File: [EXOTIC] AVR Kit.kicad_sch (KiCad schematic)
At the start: 20 parts, among them J2 AVR-ISP-10, J3 USB_B, J4 Conn_01x08_Socket, J5 Conn_01x08_Socket, J6 Conn_01x09_Socket, J7 Conn_01x07_Socket, SW1 SW_Push, U1 ATmega32A-P, U6 CH340C, Y1 16 MHz

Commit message: Update [EXOTIC] AVR Kit.kicad_sch
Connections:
- net PC0: now also J6.2 (Pin_2); no longer J6.8 (Pin_8)
- net PC1: now also J6.3 (Pin_3); no longer J6.7 (Pin_7)
- net PC6: now also J6.8 (Pin_8); no longer J6.2 (Pin_2)
- net PC7: now also J6.9 (Pin_9); no longer J6.1 (Pin_1)
- net PD7: now also J6.1 (Pin_1); no longer J6.9 (Pin_9)
- net TCK: now also J6.4 (Pin_4); no longer J6.6 (Pin_6)
- net TDI: now also J6.7 (Pin_7); no longer J6.3 (Pin_3)
- net TDO: now also J6.6 (Pin_6); no longer J6.4 (Pin_4)
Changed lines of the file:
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@@
     )
   )
-  (symbol (lib_id "Connector:Conn_01x09_Socket") (at 110.49 106.68 0) (mirror x) (unit 1)
-    (in_bom yes) (on_board yes) (dnp no) (fields_autoplaced)
-    (property "Reference" "J6" (at 111.76 105.41 0)
+  (symbol (lib_id "Connector:Conn_01x09_Socket") (at 110.49 106.68 0) (unit 1)
+    (in_bom yes) (on_board yes) (dnp no)
+    (property "Reference" "J6" (at 111.76 107.95 0)
       (effects (font (size 1.27 1.27)) (justify left))
     )
-    (property "Value" "Conn_01x09_Socket" (at 111.76 107.95 0)
+    (property "Value" "Conn_01x09_Socket" (at 111.76 105.41 0)
       (effects (font (size 1.27 1.27)) (justify left))
     )

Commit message: WIP
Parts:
- added J8: ICSP_Connector, Connector_PinHeader_2.54mm:PinHeader_2x03_P2.54mm_Vertical, symbol PCM_SL_Connectors:ICSP_Connector
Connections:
- net +5V: now also J8.2 (VCC)
- net GND: now also J8.6 (GND)
- net MISO: now also J8.1 (MISO)
- net MOSI: now also J8.4 (MOSI)
- net SCK: now also J8.3 (SCK)
- net ~{RESET}: now also J8.5 (~{RST})
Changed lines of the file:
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@@
+    (stroke (width 0) (type default))
+  )
+  (wire (pts (xy 189.23 52.07) (xy 191.77 52.07))
     (stroke (width 0) (type default))
   )
@@
     (stroke (width 0) (type default))
   )
+  (wire (pts (xy 210.82 46.99) (xy 208.28 46.99))
+    (stroke (width 0) (type default))
+  )
   (wire (pts (xy 91.44 111.76) (xy 105.41 111.76))
     (stroke (width 0) (type default))
@@
     (stroke (width 0) (type default))
   )
+  (wire (pts (xy 210.82 52.07) (xy 208.28 52.07))
+    (stroke (width 0) (type default))
+  )
   (wire (pts (xy 76.2 147.32) (xy 76.2 148.59))
     (stroke (width 0) (type default))
@@
     (stroke (width 0) (type default))
   )
+  (wire (pts (xy 189.23 46.99) (xy 191.77 46.99))
+    (stroke (width 0) (type default))
+  )
   (wire (pts (xy 58.42 44.45) (xy 60.96 44.45))
     (stroke (width 0) (type default))
@@
     (stroke (width 0) (type default))
   )
+  (wire (pts (xy 189.23 49.53) (xy 191.77 49.53))
+    (stroke (width 0) (type default))
+  )
   (wire (pts (xy 154.94 115.57) (xy 157.48 115.57))
     (stroke (width 0) (type default))
@@
   )
   (wire (pts (xy 91.44 101.6) (xy 105.41 101.6))
+    (stroke (width 0) (type default))
+  )
+  (wire (pts (xy 210.82 49.53) (xy 208.28 49.53))
     (stroke (width 0) (type default))
   )
@@
     (effects (font (size 1.27 1.27)) (justify left bottom))
   )
+  (label "MOSI" (at 210.82 49.53 0) (fields_autoplaced)
+    (effects (font (size 1.27 1.27)) (justify left bottom))
+  )
   (label "PD7" (at 101.6 96.52 0) (fields_autoplaced)
     (effects (font (size 1.27 1.27)) (justify left bottom))
@@
     (effects (font (size 1.27 1.27)) (justify left bottom))
   )
+  (label "SCK" (at 189.23 49.53 180) (fields_autoplaced)
+    (effects (font (size 1.27 1.27)) (justify right bottom))
+  )
   (label "PA3" (at 93.98 60.96 0) (fields_autoplaced)
     (effects (font (size 1.27 1.27)) (justify left bottom))
@@
   (label "PA4" (at 93.98 63.5 0) (fields_autoplaced)
     (effects (font (size 1.27 1.27)) (justify left bottom))
+  )
+  (label "MISO" (at 189.23 46.99 180) (fields_autoplaced)
+    (effects (font (size 1.27 1.27)) (justify right bottom))
   )
   (label "TDO" (at 93.98 109.22 0) (fields_autoplaced)
@@
   (label "PB1" (at 93.98 78.74 0) (fields_autoplaced)
     (effects (font (size 1.27 1.27)) (justify left bottom))
+  )
+  (label "~{RESET}" (at 189.23 52.07 180) (fields_autoplaced)
+    (effects (font (size 1.27 1.27)) (justify right bottom))
   )
   (label "~{RESET}" (at 55.88 53.34 180) (fields_autoplaced)
@@
     )
   )
+  (symbol (lib_id "PCM_SL_Connectors:ICSP_Connector") (at 199.39 49.53 0) (unit 1)
+    (in_bom yes) (on_board yes) (dnp no) (fields_autoplaced)
+    (property "Reference" "J8" (at 201.93 39.37 0)
+      (effects (font (size 1.27 1.27)))
+    )
+    (property "Value" "ICSP_Connector" (at 201.93 41.91 0)
+      (effects (font (size 1.27 1.27)))
+    )
+    (property "Footprint" "Connector_PinHeader_2.54mm:PinHeader_2x03_P2.54mm_Vertical" (at 195.58 46.99 0)
+      (effects (font (size 1.27 1.27)) hide)
+    )
+    (property "Datasheet" "" (at 195.58 46.99 0)
+      (effects (font (size 1.27 1.27)) hide)
+    )
+    (pin "3")
+    (pin "6")
+    (pin "5")
+    (pin "1")
+    (pin "4")
+    (pin "2")
+    (instances
+      (project "[EXOTIC] AVR Kit"
+        (path "/bd689b4b-40d7-46ba-91b6-965ce30f8212"
+          (reference "J8") (unit 1)
+        )
+      )
+    )
+  )
   (symbol (lib_id "Device:R") (at 60.96 35.56 0) (unit 1)
     (in_bom yes) (on_board yes) (dnp no) (fields_autoplaced)
@@
     )
   )
+  (symbol (lib_id "power:GND") (at 210.82 52.07 0) (unit 1)
+    (in_bom yes) (on_board yes) (dnp no) (fields_autoplaced)
+    (property "Reference" "#PWR033" (at 210.82 58.42 0)
+      (effects (font (size 1.27 1.27)) hide)
+    )
+    (property "Value" "GND" (at 210.82 57.15 0)
+      (effects (font (size 1.27 1.27)))
+    )
+    (property "Footprint" "" (at 210.82 52.07 0)
+      (effects (font (size 1.27 1.27)) hide)
+    )
+    (property "Datasheet" "" (at 210.82 52.07 0)
+      (effects (font (size 1.27 1.27)) hide)
+    )
+    (pin "1")
+    (instances
+      (project "[EXOTIC] AVR Kit"
+        (path "/bd689b4b-40d7-46ba-91b6-965ce30f8212"
+          (reference "#PWR033") (unit 1)
+        )
+      )
+      (project "ATMEGA32A Development Board"
+        (path "/e232854a-3fe0-4443-9abe-081b69d86c79"
+          (reference "#PWR018") (unit 1)
+        )
+      )
+    )
+  )
   (symbol (lib_id "Connector:USB_B") (at 199.39 102.87 0) (mirror y) (unit 1)
     (in_bom yes) (on_board yes) (dnp no)
@@
         )
       )
+    )
+  )
+  (symbol (lib_id "power:+5V") (at 210.82 46.99 0) (unit 1)
+    (in_bom yes) (on_board yes) (dnp no) (fields_autoplaced)
+    (property "Reference" "#PWR032" (at 210.82 50.8 0)
+      (effects (font (size 1.27 1.27)) hide)
+    )
+    (property "Value" "+5V" (at 210.82 43.18 0)
+      (effects (font (size 1.27 1.27)))
+    )
+    (property "Footprint" "" (at 210.82 46.99 0)
+      (effects (font (size 1.27 1.27)) hide)
+    )
+    (property "Datasheet" "" (at 210.82 46.99 0)
+      (effects (font (size 1.27 1.27)) hide)
+    )
+    (pin "1")
+    (instances
+      (project "[EXOTIC] AVR Kit"
+        (path "/bd689b4b-40d7-46ba-91b6-965ce30f8212"
+          (reference "#PWR032") (unit 1)
+        )
+      )
+      (project "ATMEGA32A Development Board"
+        (path "/e232854a-3fe0-4443-9abe-081b69d86c79"
+          (reference "#PWR012") (unit 1)
+        )
+      )

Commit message: Rev. 3
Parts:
- removed J8: ICSP_Connector, Connector_PinHeader_2.54mm:PinHeader_2x03_P2.54mm_Vertical, symbol PCM_SL_Connectors:ICSP_Connector
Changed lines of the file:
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@@
-    (stroke (width 0) (type default))
-  )
-  (wire (pts (xy 189.23 52.07) (xy 191.77 52.07))
     (stroke (width 0) (type default))
   )
@@
     (stroke (width 0) (type default))
   )
-  (wire (pts (xy 210.82 46.99) (xy 208.28 46.99))
-    (stroke (width 0) (type default))
-  )
   (wire (pts (xy 91.44 111.76) (xy 105.41 111.76))
     (stroke (width 0) (type default))
@@
     (stroke (width 0) (type default))
   )
-  (wire (pts (xy 210.82 52.07) (xy 208.28 52.07))
-    (stroke (width 0) (type default))
-  )
   (wire (pts (xy 76.2 147.32) (xy 76.2 148.59))
     (stroke (width 0) (type default))
@@
     (stroke (width 0) (type default))
   )
-  (wire (pts (xy 189.23 46.99) (xy 191.77 46.99))
-    (stroke (width 0) (type default))
-  )
   (wire (pts (xy 58.42 44.45) (xy 60.96 44.45))
     (stroke (width 0) (type default))
@@
     (stroke (width 0) (type default))
   )
-  (wire (pts (xy 189.23 49.53) (xy 191.77 49.53))
-    (stroke (width 0) (type default))
-  )
   (wire (pts (xy 154.94 115.57) (xy 157.48 115.57))
     (stroke (width 0) (type default))
@@
   )
   (wire (pts (xy 91.44 101.6) (xy 105.41 101.6))
-    (stroke (width 0) (type default))
-  )
-  (wire (pts (xy 210.82 49.53) (xy 208.28 49.53))
     (stroke (width 0) (type default))
   )
@@
     (effects (font (size 1.27 1.27)) (justify left bottom))
   )
-  (label "MOSI" (at 210.82 49.53 0) (fields_autoplaced)
-    (effects (font (size 1.27 1.27)) (justify left bottom))
-  )
   (label "PD7" (at 101.6 96.52 0) (fields_autoplaced)
     (effects (font (size 1.27 1.27)) (justify left bottom))
@@
     (effects (font (size 1.27 1.27)) (justify left bottom))
   )
-  (label "SCK" (at 189.23 49.53 180) (fields_autoplaced)
-    (effects (font (size 1.27 1.27)) (justify right bottom))
-  )
   (label "PA3" (at 93.98 60.96 0) (fields_autoplaced)
     (effects (font (size 1.27 1.27)) (justify left bottom))
@@
   (label "PA4" (at 93.98 63.5 0) (fields_autoplaced)
     (effects (font (size 1.27 1.27)) (justify left bottom))
-  )
-  (label "MISO" (at 189.23 46.99 180) (fields_autoplaced)
-    (effects (font (size 1.27 1.27)) (justify right bottom))
   )
   (label "TDO" (at 93.98 109.22 0) (fields_autoplaced)
@@
   (label "PB1" (at 93.98 78.74 0) (fields_autoplaced)
     (effects (font (size 1.27 1.27)) (justify left bottom))
-  )
-  (label "~{RESET}" (at 189.23 52.07 180) (fields_autoplaced)
-    (effects (font (size 1.27 1.27)) (justify right bottom))
   )
   (label "~{RESET}" (at 55.88 53.34 180) (fields_autoplaced)
@@
     )
   )
-  (symbol (lib_id "PCM_SL_Connectors:ICSP_Connector") (at 199.39 49.53 0) (unit 1)
-    (in_bom yes) (on_board yes) (dnp no) (fields_autoplaced)
-    (property "Reference" "J8" (at 201.93 39.37 0)
-      (effects (font (size 1.27 1.27)))
-    )
-    (property "Value" "ICSP_Connector" (at 201.93 41.91 0)
-      (effects (font (size 1.27 1.27)))
-    )
-    (property "Footprint" "Connector_PinHeader_2.54mm:PinHeader_2x03_P2.54mm_Vertical" (at 195.58 46.99 0)
-      (effects (font (size 1.27 1.27)) hide)
-    )
-    (property "Datasheet" "" (at 195.58 46.99 0)
-      (effects (font (size 1.27 1.27)) hide)
-    )
-    (pin "3")
-    (pin "6")
-    (pin "5")
-    (pin "1")
-    (pin "4")
-    (pin "2")
-    (instances
-      (project "[EXOTIC] AVR Kit"
-        (path "/bd689b4b-40d7-46ba-91b6-965ce30f8212"
-          (reference "J8") (unit 1)
-        )
-      )
-    )
-  )
   (symbol (lib_id "Device:R") (at 60.96 35.56 0) (unit 1)
     (in_bom yes) (on_board yes) (dnp no) (fields_autoplaced)
@@
     )
   )
-  (symbol (lib_id "power:GND") (at 210.82 52.07 0) (unit 1)
-    (in_bom yes) (on_board yes) (dnp no) (fields_autoplaced)
-    (property "Reference" "#PWR033" (at 210.82 58.42 0)
-      (effects (font (size 1.27 1.27)) hide)
-    )
-    (property "Value" "GND" (at 210.82 57.15 0)
-      (effects (font (size 1.27 1.27)))
-    )
-    (property "Footprint" "" (at 210.82 52.07 0)
-      (effects (font (size 1.27 1.27)) hide)
-    )
-    (property "Datasheet" "" (at 210.82 52.07 0)
-      (effects (font (size 1.27 1.27)) hide)
-    )
-    (pin "1")
-    (instances
-      (project "[EXOTIC] AVR Kit"
-        (path "/bd689b4b-40d7-46ba-91b6-965ce30f8212"
-          (reference "#PWR033") (unit 1)
-        )
-      )
-      (project "ATMEGA32A Development Board"
-        (path "/e232854a-3fe0-4443-9abe-081b69d86c79"
-          (reference "#PWR018") (unit 1)
-        )
-      )
-    )
-  )
   (symbol (lib_id "Connector:USB_B") (at 199.39 102.87 0) (mirror y) (unit 1)
     (in_bom yes) (on_board yes) (dnp no)
@@
         )
       )
-    )
-  )
-  (symbol (lib_id "power:+5V") (at 210.82 46.99 0) (unit 1)
-    (in_bom yes) (on_board yes) (dnp no) (fields_autoplaced)
-    (property "Reference" "#PWR032" (at 210.82 50.8 0)
-      (effects (font (size 1.27 1.27)) hide)
-    )
-    (property "Value" "+5V" (at 210.82 43.18 0)
-      (effects (font (size 1.27 1.27)))
-    )
-    (property "Footprint" "" (at 210.82 46.99 0)
-      (effects (font (size 1.27 1.27)) hide)
-    )
-    (property "Datasheet" "" (at 210.82 46.99 0)
-      (effects (font (size 1.27 1.27)) hide)
-    )
-    (pin "1")
-    (instances
-      (project "[EXOTIC] AVR Kit"
-        (path "/bd689b4b-40d7-46ba-91b6-965ce30f8212"
-          (reference "#PWR032") (unit 1)
-        )
-      )
-      (project "ATMEGA32A Development Board"
-        (path "/e232854a-3fe0-4443-9abe-081b69d86c79"
-          (reference "#PWR012") (unit 1)
-        )
-      )

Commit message: Rev 3.2
Cleaned Up Schematic
Revised Layout
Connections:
- net +5V: no longer J2.2 (VCC), L1.2
- new net +5V_NetTie: J2.2 (VCC), L1.2
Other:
- note added: "AVR"
- note added: "ISP Interface"
- note added: "USB Interface"
- moved on the sheet: C1, C10, C11, C12, C2, C3, C4, C9, J2, J3, J4, J5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

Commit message: Schematic Organization
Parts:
- J4: value Conn_01x08_Socket -> Port A
- J5: value Conn_01x08_Socket -> Port B
- J6: value Conn_01x09_Socket -> Port C + D7
- J7: value Conn_01x07_Socket -> Port D
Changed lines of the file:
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@@
+    (fill (type none))
+  )
+  (rectangle (start 139.7 88.9) (end 284.48 152.4)
+    (stroke (width 0) (type default))
     (fill (type none))
   )
@@
   )
   (text "Rx and TX labels and arrows are from the prespective of the 32A\nCheck USB Shield Coonnection (Should it tie to ground ?)"
-    (at 177.8 165.1 0)
+    (at 110.49 195.58 0)
     (effects (font (size 1.27 1.27)) (justify left bottom))
   )
@@
       (effects (font (size 1.27 1.27)) (justify left))
     )
-    (property "Value" "Conn_01x08_Socket" (at 111.76 80.01 0)
+    (property "Value" "Port B" (at 111.76 80.01 0)
       (effects (font (size 1.27 1.27)) (justify left))
     )
@@
       (effects (font (size 1.27 1.27)) (justify left))
     )
-    (property "Value" "Conn_01x09_Socket" (at 111.76 99.06 0)
+    (property "Value" "Port C + D7" (at 111.76 99.06 0)
       (effects (font (size 1.27 1.27)) (justify left))
     )
@@
       (effects (font (size 1.27 1.27)) (justify left))
     )
-    (property "Value" "Conn_01x08_Socket" (at 111.76 57.15 0)
+    (property "Value" "Port A" (at 111.76 57.15 0)
       (effects (font (size 1.27 1.27)) (justify left))
     )
@@
       (effects (font (size 1.27 1.27)) (justify left))
     )
-    (property "Value" "Conn_01x07_Socket" (at 111.76 124.46 0)
-      (effects (font (size 1.27 1.27)) (justify left))
-    )
+    (property "Value" "Port D" (at 111.76 124.46 0)
+      (effects (font (size 1.27 1.27)) (justify left))
+    )

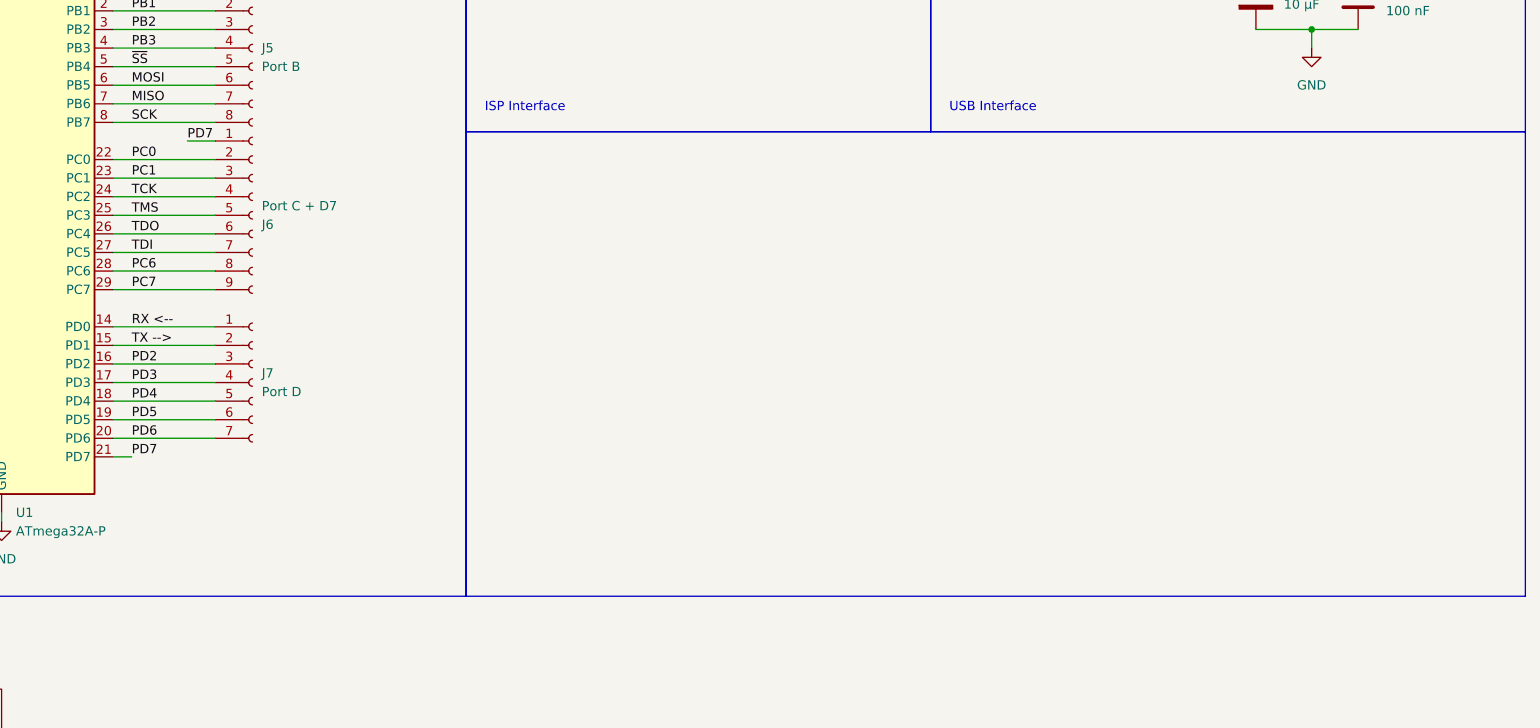
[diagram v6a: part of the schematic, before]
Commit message: Added I2C Labels
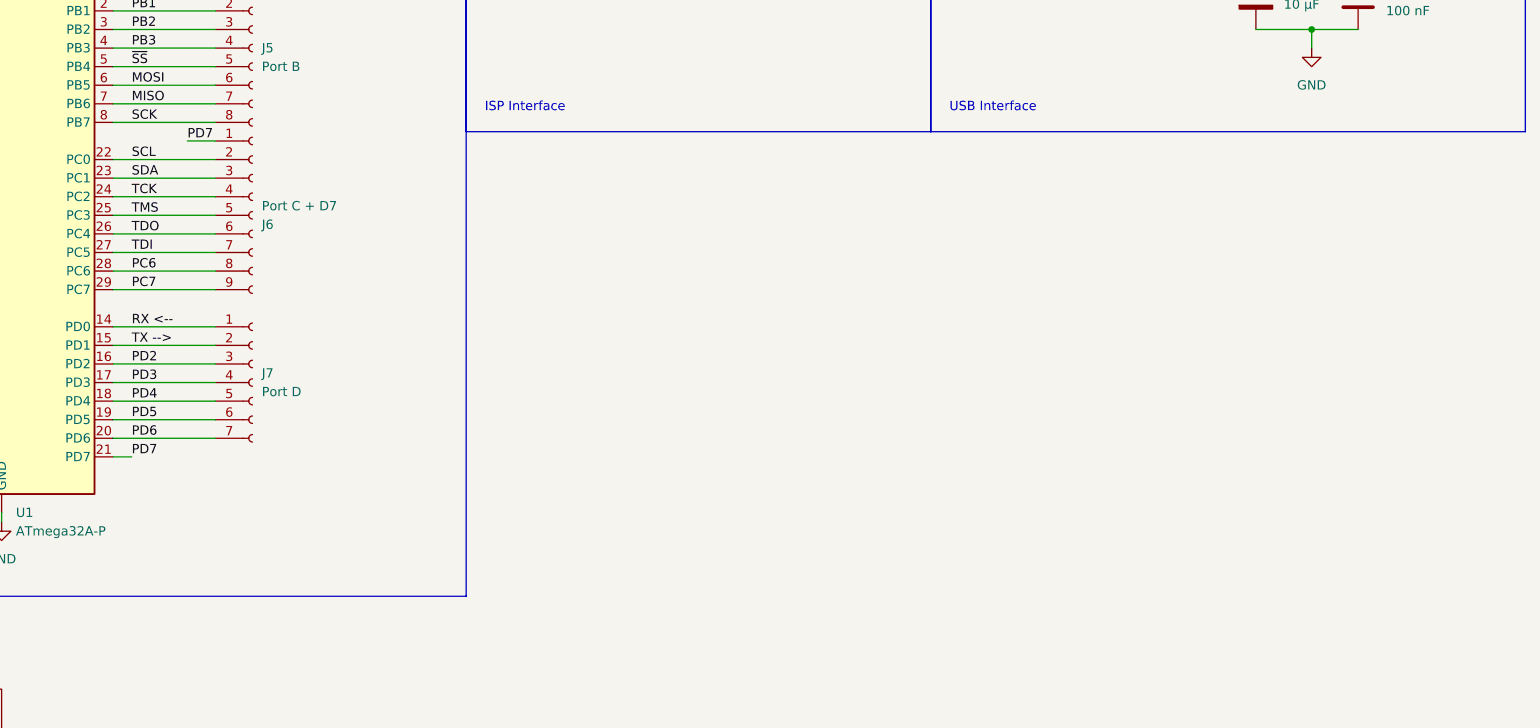
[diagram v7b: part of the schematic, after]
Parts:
- Y1: Local Seller https://makerselectronics.com/product/smd-crystal-16mhz-49s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 -> https://makerselectronics.com/product/crystal-16-000mhz-49s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
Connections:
- net PC0 renamed SCL
- net PC1 renamed SDA
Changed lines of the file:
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@@
-    (fill (type none))
-  )
-  (rectangle (start 139.7 88.9) (end 284.48 152.4)
-    (stroke (width 0) (type default))
     (fill (type none))
   )
@@
     (effects (font (size 1.27 1.27)) (justify left bottom))
   )
-  (label "PC1" (at 93.98 95.25 0) (fields_autoplaced)
-    (effects (font (size 1.27 1.27)) (justify left bottom))
-  )
-  (label "PC0" (at 93.98 92.71 0) (fields_autoplaced)
+  (label "SDA" (at 93.98 95.25 0) (fields_autoplaced)
+    (effects (font (size 1.27 1.27)) (justify left bottom))
+  )
+  (label "SCL" (at 93.98 92.71 0) (fields_autoplaced)
     (effects (font (size 1.27 1.27)) (justify left bottom))
   )
@@
       (effects (font (size 1.27 1.27)) hide)
     )
-    (property "Local Seller" "https://makerselectronics.com/product/smd-crystal-16mhz-49smd" (at 48.26 54.61 0)
-      (effects (font (size 1.27 1.27)) hide)
-    )
+    (property "Local Seller" "https://makerselectronics.com/product/crystal-16-000mhz-49s-20ppm-20pf-40%cf%89" (at 48.26 54.61 0)
+      (effects (font (size 1.27 1.27)) hide)
+    )
